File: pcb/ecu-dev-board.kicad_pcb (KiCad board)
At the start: 4 copper layers, 99.9 x 99.9 mm, 258 parts, among them IC201 MAX9924UAUB+, IC401 74HC14D-Q100,118, IC601 UCC28910DR, IC701 UCC27624DR, J101 MX23A18NF1, J102 39-30-1020, K501 Relay, Q201 MMBT2222A, Q501 MMBT2222A, Q502 MMBTA55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

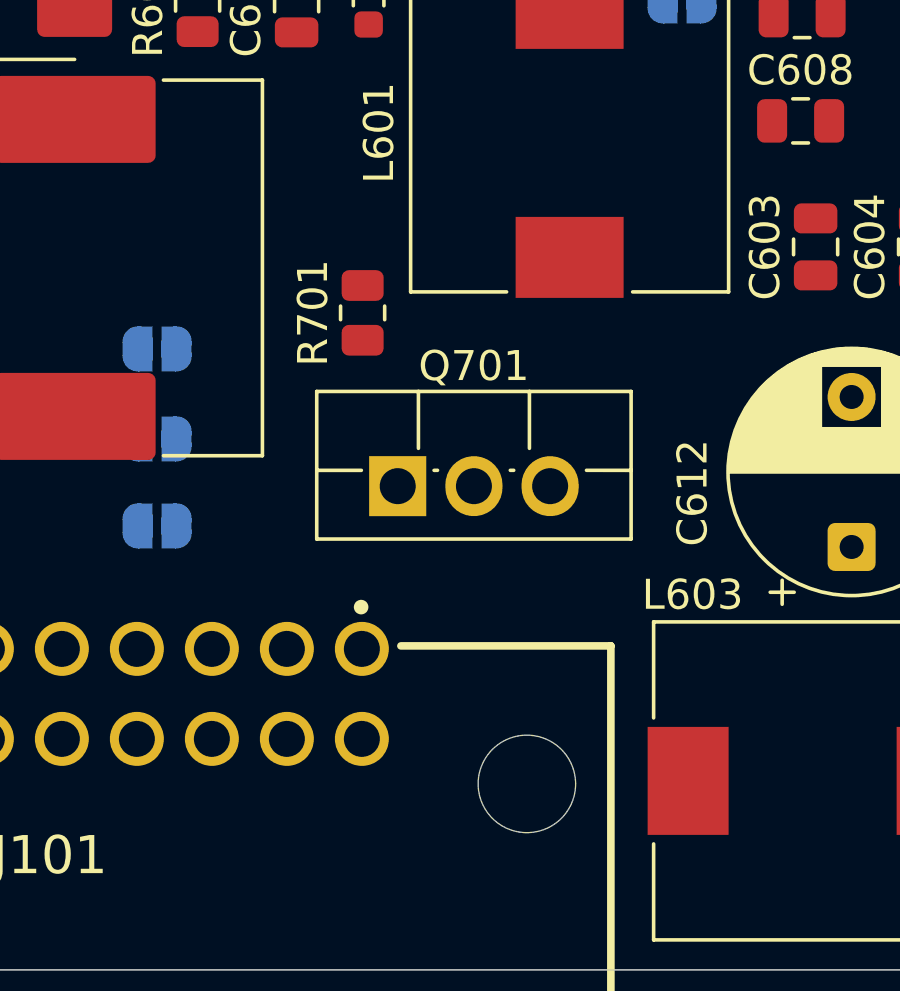
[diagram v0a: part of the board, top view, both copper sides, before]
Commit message: changed battery pin with coil qs
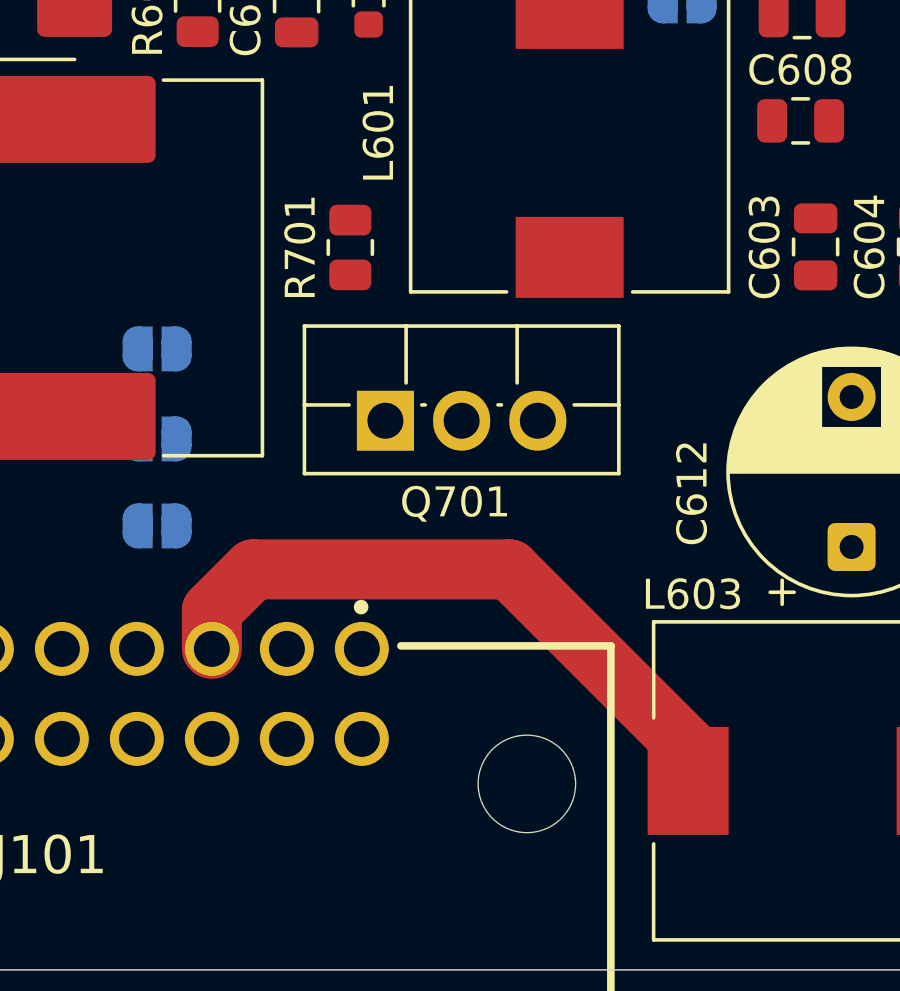
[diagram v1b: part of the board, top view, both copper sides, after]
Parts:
- moved Q701 2.22 mm to (213.7, 117.6)
- moved R701 2.22 mm to (212.5, 111.8)
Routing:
- net +BATT: track 0.00 -> 21.3 mm
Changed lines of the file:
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@@
 				(font
 					(size 0.001 0.001)
+					(thickness 0.15)
 				)
 			)
@@
 				(font
 					(size 0.001 0.001)
+					(thickness 0.15)
 				)
 			)
@@
 				(font
 					(size 0.001 0.001)
+					(thickness 0.15)
 				)
 			)
@@
 				(font
 					(size 0.001 0.001)
+					(thickness 0.15)
 				)
 			)
@@
 				(font
 					(size 0.001 0.001)
+					(thickness 0.15)
 				)
 			)
@@
 				(font
 					(size 0.001 0.001)
+					(thickness 0.15)
 				)
 			)
@@
 				(font
 					(size 0.001 0.001)
+					(thickness 0.15)
 				)
 			)
@@
 				(font
 					(size 0.001 0.001)
+					(thickness 0.15)
 				)
 			)
@@
 				(font
 					(size 0.001 0.001)
+					(thickness 0.15)
 				)
 			)
@@
 				(font
 					(size 0.001 0.001)
+					(thickness 0.15)
 				)
 			)
@@
 				(font
 					(size 0.001 0.001)
+					(thickness 0.15)
 				)
 			)
@@
 				(font
 					(size 0.001 0.001)
+					(thickness 0.15)
 				)
 			)
@@
 				(font
 					(size 0.001 0.001)
+					(thickness 0.15)
 				)
 			)
@@
 				(font
 					(size 0.001 0.001)
+					(thickness 0.15)
 				)
 			)
@@
 				(font
 					(size 0.001 0.001)
+					(thickness 0.15)
 				)
 			)
@@
 				(font
 					(size 0.001 0.001)
+					(thickness 0.15)
 				)
 			)
@@
 				(font
 					(size 0.001 0.001)
+					(thickness 0.15)
 				)
 			)
@@
 				(font
 					(size 0.001 0.001)
+					(thickness 0.15)
 				)
 			)
@@
 	(footprint "Package_TO_SOT_THT:TO-220F-3_Vertical"
 		(layer "F.Cu")
-		(at 214.07 119.775)
+		(at 213.66 117.595)
 		(descr "TO-220F-3, Vertical, RM 2.54mm, see http://www.st.com/resource/en/datasheet/stp20nm60.pdf, generated with kicad-footprint-generator TO_SOT_THT_generate.py")
 		(tags "TO-220F-3 Vertical RM 2.54mm")
 		(property "Reference" "Q701"
-			(at 2.54 -4 0)
+			(at 2.33 2.725 0)
 			(layer "F.SilkS")
 			(effects
@@
 				(font
 					(size 0.001 0.001)
+					(thickness 0.15)
 				)
 			)
@@
 				(font
 					(size 0.001 0.001)
+					(thickness 0.15)
 				)
 			)
@@
 				(font
 					(size 0.001 0.001)
+					(thickness 0.15)
 				)
 			)
@@
 				(font
 					(size 0.001 0.001)
+					(thickness 0.15)
 				)
 			)
@@
 	(footprint "Resistor_SMD:R_0805_2012Metric"
 		(layer "F.Cu")
-		(at 212.9 114 90)
+		(at 212.49 111.82 90)
 		(descr "Resistor SMD 0805 (2012 Metric), square (rectangular) end terminal, IPC-7351 nominal, (Body size source: IPC-SM-782 page 72, https://www.pcb-3d.com/wordpress/wp-content/uploads/ipc-sm-782a_amendment_1_and_2.pdf), generated with kicad-footprint-generator")
 		(tags "resistor")
@@
 				(font
 					(size 0.001 0.001)
+					(thickness 0.15)
 				)
 			)
@@
 				(font
 					(size 0.001 0.001)
+					(thickness 0.15)
 				)
 			)
@@
 				(font
 					(size 0.001 0.001)
+					(thickness 0.15)
 				)
 				(justify mirror)
@@
 				(font
 					(size 0.001 0.001)
+					(thickness 0.15)
 				)
 				(justify mirror)
@@
 				(font
 					(size 0.001 0.001)
+					(thickness 0.15)
 				)
 				(justify mirror)
@@
 				(font
 					(size 0.001 0.001)
+					(thickness 0.15)
 				)
 				(justify mirror)
@@
 				(font
 					(size 0.001 0.001)
+					(thickness 0.15)
 				)
 				(justify mirror)
@@
 				(font
 					(size 0.001 0.001)
+					(thickness 0.15)
 				)
 				(justify mirror)
@@
 				(font
 					(size 0.001 0.001)
+					(thickness 0.15)
 				)
 				(justify mirror)
@@
 				(font
 					(size 0.001 0.001)
+					(thickness 0.15)
 				)
 				(justify mirror)
@@
 				(font
 					(size 0.001 0.001)
+					(thickness 0.15)
 				)
 				(justify mirror)
@@
 				(font
 					(size 0.001 0.001)
+					(thickness 0.15)
 				)
 				(justify mirror)
@@
 				(font
 					(size 0.001 0.001)
+					(thickness 0.15)
 				)
 				(justify mirror)
@@
 				(font
 					(size 0.001 0.001)
+					(thickness 0.15)
 				)
 				(justify mirror)
@@
 				(font
 					(size 0.001 0.001)
+					(thickness 0.15)
 				)
 				(justify mirror)
@@
 				(font
 					(size 0.001 0.001)
+					(thickness 0.15)
 				)
 				(justify mirror)
@@
 				(font
 					(size 0.001 0.001)
+					(thickness 0.15)
 				)
 				(justify mirror)
@@
 				(font
 					(size 0.001 0.001)
+					(thickness 0.15)
 				)
 				(justify mirror)
@@
 				(font
 					(size 0.001 0.001)
+					(thickness 0.15)
 				)
 				(justify mirror)
@@
 				(font
 					(size 0.001 0.001)
+					(thickness 0.15)
 				)
 				(justify mirror)
@@
 				(font
 					(size 0.001 0.001)
+					(thickness 0.15)
 				)
 				(justify mirror)
@@
 				(font
 					(size 0.001 0.001)
+					(thickness 0.15)
 				)
 				(justify mirror)
@@
 				(font
 					(size 0.001 0.001)
+					(thickness 0.15)
 				)
 				(justify mirror)
@@
 				(font
 					(size 0.001 0.001)
+					(thickness 0.15)
 				)
 				(justify mirror)
@@
 				(font
 					(size 0.001 0.001)
+					(thickness 0.15)
 				)
 				(justify mirror)
@@
 				(font
 					(size 0.001 0.001)
+					(thickness 0.15)
 				)
 				(justify mirror)
@@
 				(font
 					(size 0.001 0.001)
+					(thickness 0.15)
 				)
 				(justify mirror)
@@
 				(font
 					(size 0.001 0.001)
+					(thickness 0.15)
 				)
 				(justify mirror)
@@
 				(font
 					(size 0.001 0.001)
+					(thickness 0.15)
 				)
 				(justify mirror)
@@
 				(font
 					(size 0.001 0.001)
+					(thickness 0.15)
 				)
 				(justify mirror)
@@
 				(font
 					(size 0.001 0.001)
+					(thickness 0.15)
 				)
 				(justify mirror)
@@
 				(font
 					(size 0.001 0.001)
+					(thickness 0.15)
 				)
 				(justify mirror)
@@
 		(net 3)
 	)
+	(segment
+		(start 207.875 123.927208)
+		(end 209.252208 122.55)
+		(width 2)
+		(layer "F.Cu")
+		(net 111)
+	)
+	(segment
+		(start 217.8 122.55)
+		(end 223.75 128.5)
+		(width 2)
+		(layer "F.Cu")
+		(net 111)
+	)
+	(segment
+		(start 209.252208 122.55)
+		(end 217.8 122.55)
+		(width 2)
+		(layer "F.Cu")
+		(net 111)
+	)
+	(segment
+		(start 207.875 125.2)
+		(end 207.875 123.927208)
+		(width 2)
+		(layer "F.Cu")
+		(net 111)
+	)
+	(segment
+		(start 223.75 128.5)
+		(end 223.75 129.6)
+		(width 2)
+		(layer "F.Cu")
+		(net 111)
+	)
 	(embedded_fonts no)

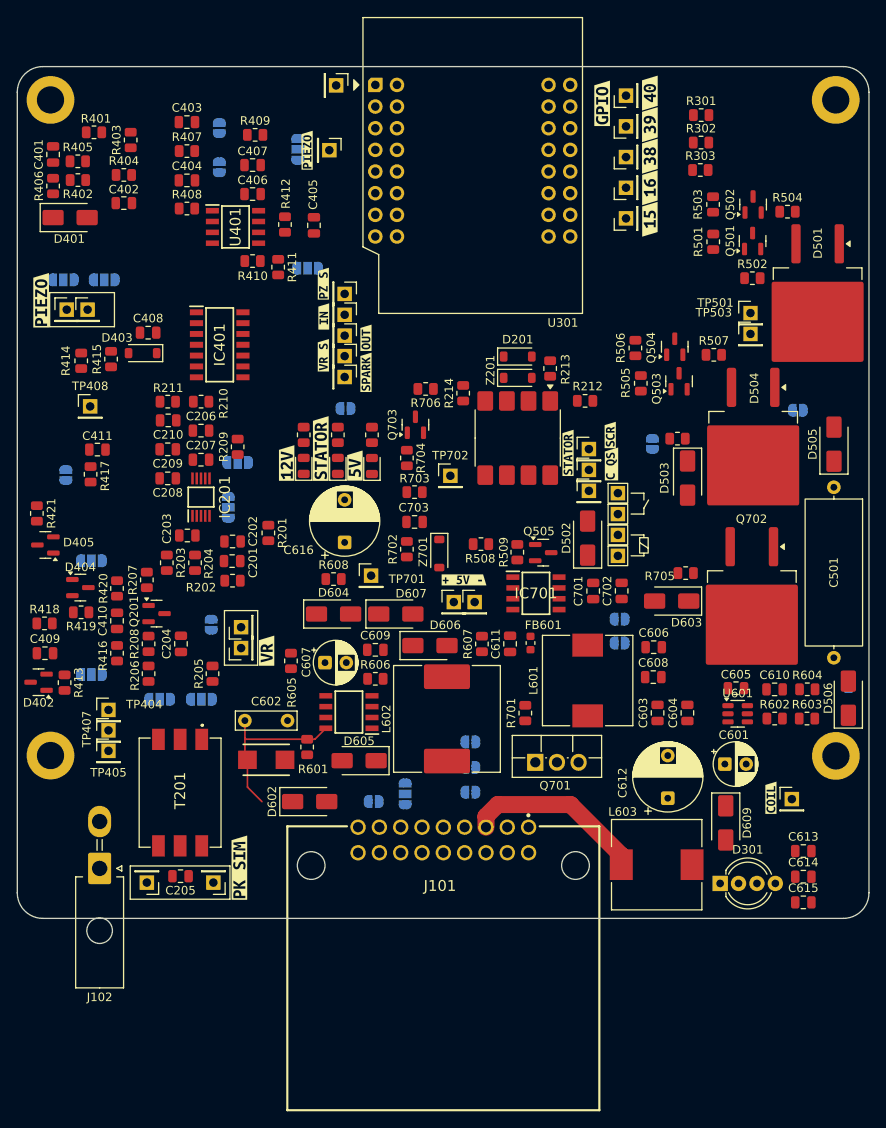
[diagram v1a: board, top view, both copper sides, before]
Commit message: routed 5V
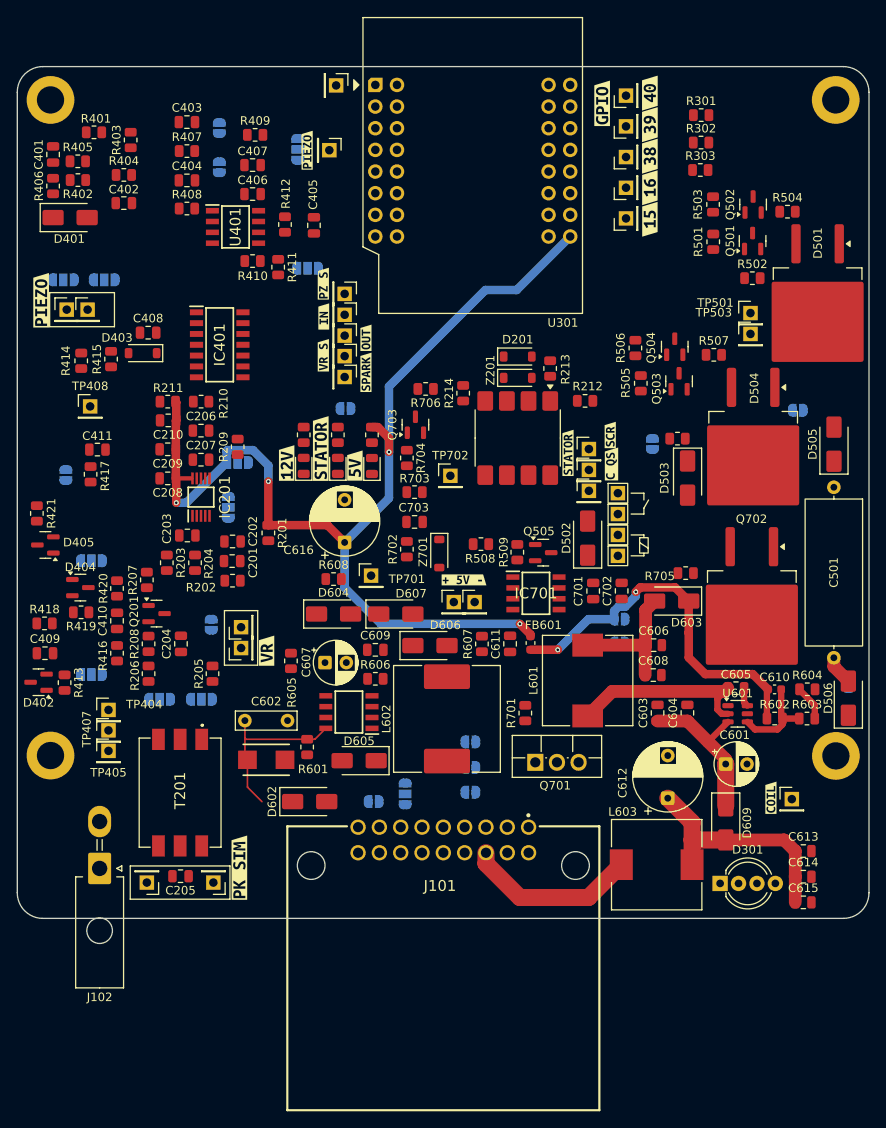
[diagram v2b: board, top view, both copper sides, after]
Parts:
- C610: footprint Capacitor_SMD:C_0805_2012Metric -> Capacitor_SMD:C_0603_1608Metric
- moved C606 0.24 mm to (227.6, 103.8)
- moved C608 0.24 mm to (227.5, 107.4)
- moved C601 0.10 mm to (236.0, 117.8)
- renumbered 06 to JP206, 07 to JP207, 08 to JP208, 604 to JP604, 605 to JP605
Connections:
- J101 pad 12: COIL_QS -> +BATT
- J101 pad 3: +BATT -> COIL_QS
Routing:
- net +5V: track 0.00 -> 128.2 mm, vias 0 -> 4
- net /PSU/FB_5: track 0.00 -> 44.1 mm, vias 0 -> 2
- net Net-(D609-A): track 0.00 -> 27.6 mm
- net Net-(U601-SW): track 0.00 -> 22.3 mm
- net +12V: track 0.00 -> 18.6 mm
- net Net-(D603-A): track 0.00 -> 15.9 mm
- net Net-(U601-FB): track 0.00 -> 10.9 mm
- net Net-(R603-Pad2): track 0.00 -> 4.17 mm
- net COIL: track 0.00 -> 3.44 mm
- net Net-(U601-BOOT): track 0.00 -> 2.21 mm
- net +BATT: track 21.3 -> 20.4 mm

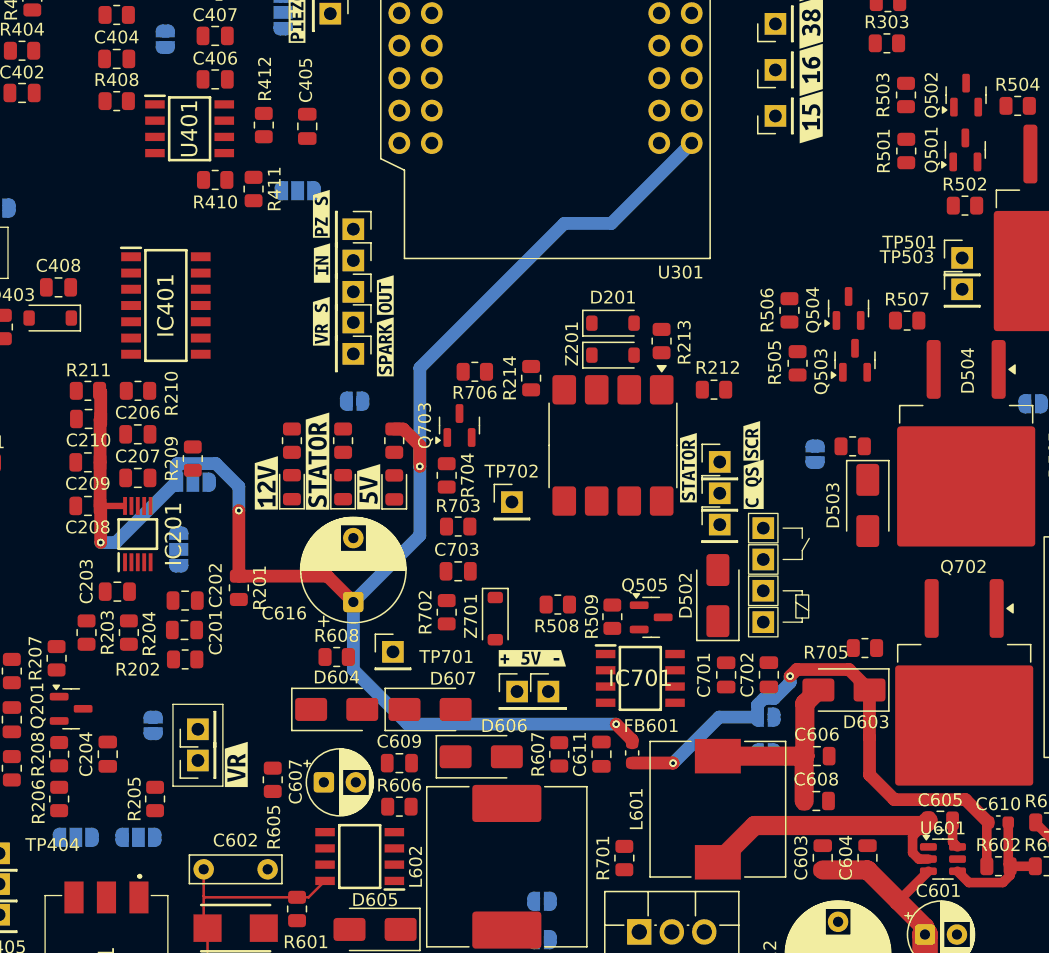
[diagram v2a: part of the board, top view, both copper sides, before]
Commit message: routed 12V
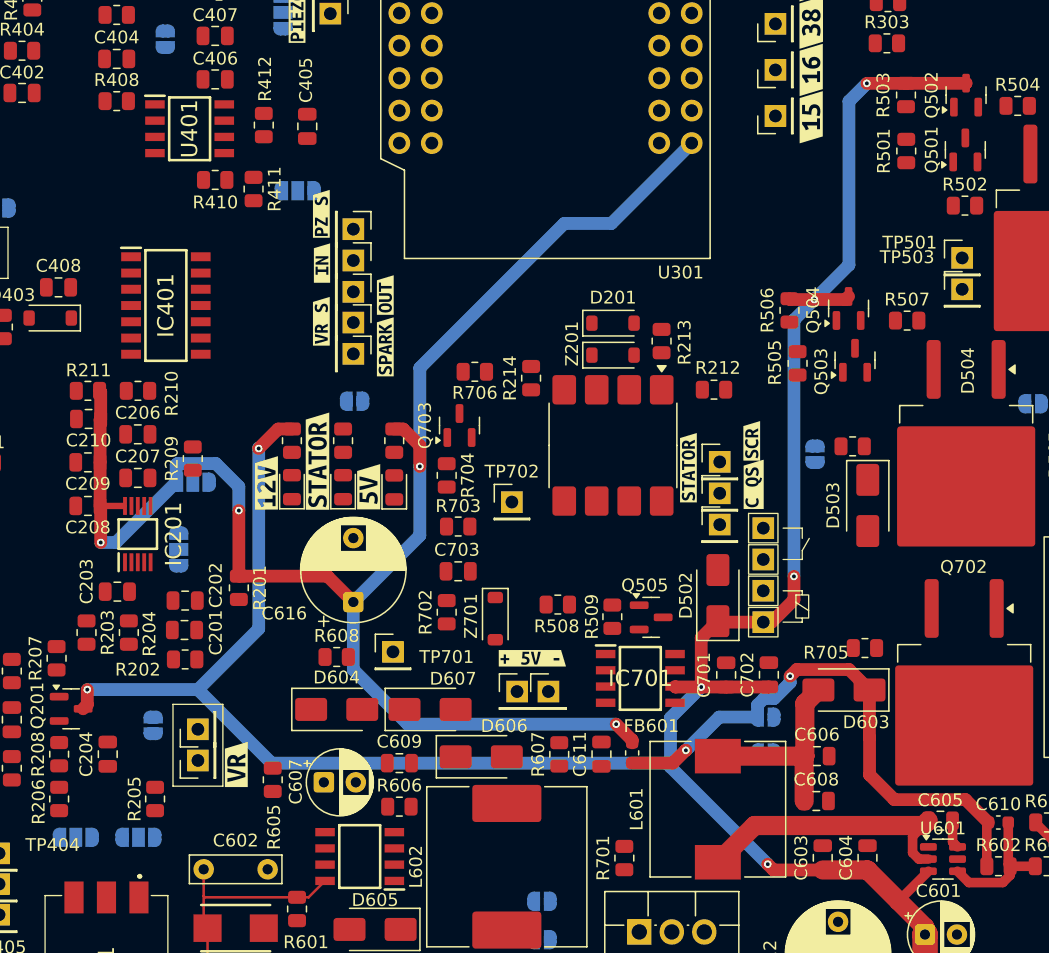
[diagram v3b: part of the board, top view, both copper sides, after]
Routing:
- net +12V: track 18.6 -> 189.9 mm, vias 0 -> 7

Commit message: routed 3V3
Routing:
- net +3V3: track 0.00 -> 153.8 mm, vias 0 -> 6
